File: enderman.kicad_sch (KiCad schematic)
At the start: 22 parts, among them U1 4030, U2 LM556

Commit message: v2.0 RTM
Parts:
- removed R2: 4k7, Resistor_SMD:R_0603_1608Metric, symbol Device:R
- removed R3: 5k1, Resistor_SMD:R_0603_1608Metric, symbol Device:R
- added LS1: Speaker_Crystal, Library:Piezo PKMCS0909E4000-R1, symbol Device:Speaker_Crystal
- added R2, R3: R_Photo, Library:SMD2.4x3.6, symbol Device:R_Photo
- BT1, BT2, BT3: footprint Library:BatteryHolder_Keystone_3030 -> Library:BatteryHolder_Keystone_2996; Digikey 36-3034-ND -> 36-2996-ND
- C2, C5: value 1u -> 47n; LCSC C15849 -> C1622
- D1, D2: LCSC (none) -> C7371915
- U1: LCSC (none) -> C458786
- U2: LCSC (none) -> C18164404
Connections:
- net +6V: now also U1.13, U1.9, R2.1, R3.1; no longer U1.6
- net GND: now also U1.1, U1.2, LS1.2; no longer U1.12, U1.13, U1.8, U1.9
- net at U1.4: now also D1.1 (K), U1.12, U1.8; no longer D2.1 (K)
- net at R1.1, U2.13 (DIS): now also R2.2
- net at U2.9 (Q): now also U1.6; no longer U1.1
- net at R4.1, U2.1 (DIS): now also R3.2
- net at U2.5 (Q): now also U1.5; no longer U1.2
- net at U1.10: now also D2.1 (K)
- net at U1.11: now also LS1.1
- now unconnected: U1.3
- no-connect marks 4 -> 3
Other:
- moved on the sheet: C7, D1, R5, U1A, U1B, U1C, U1D

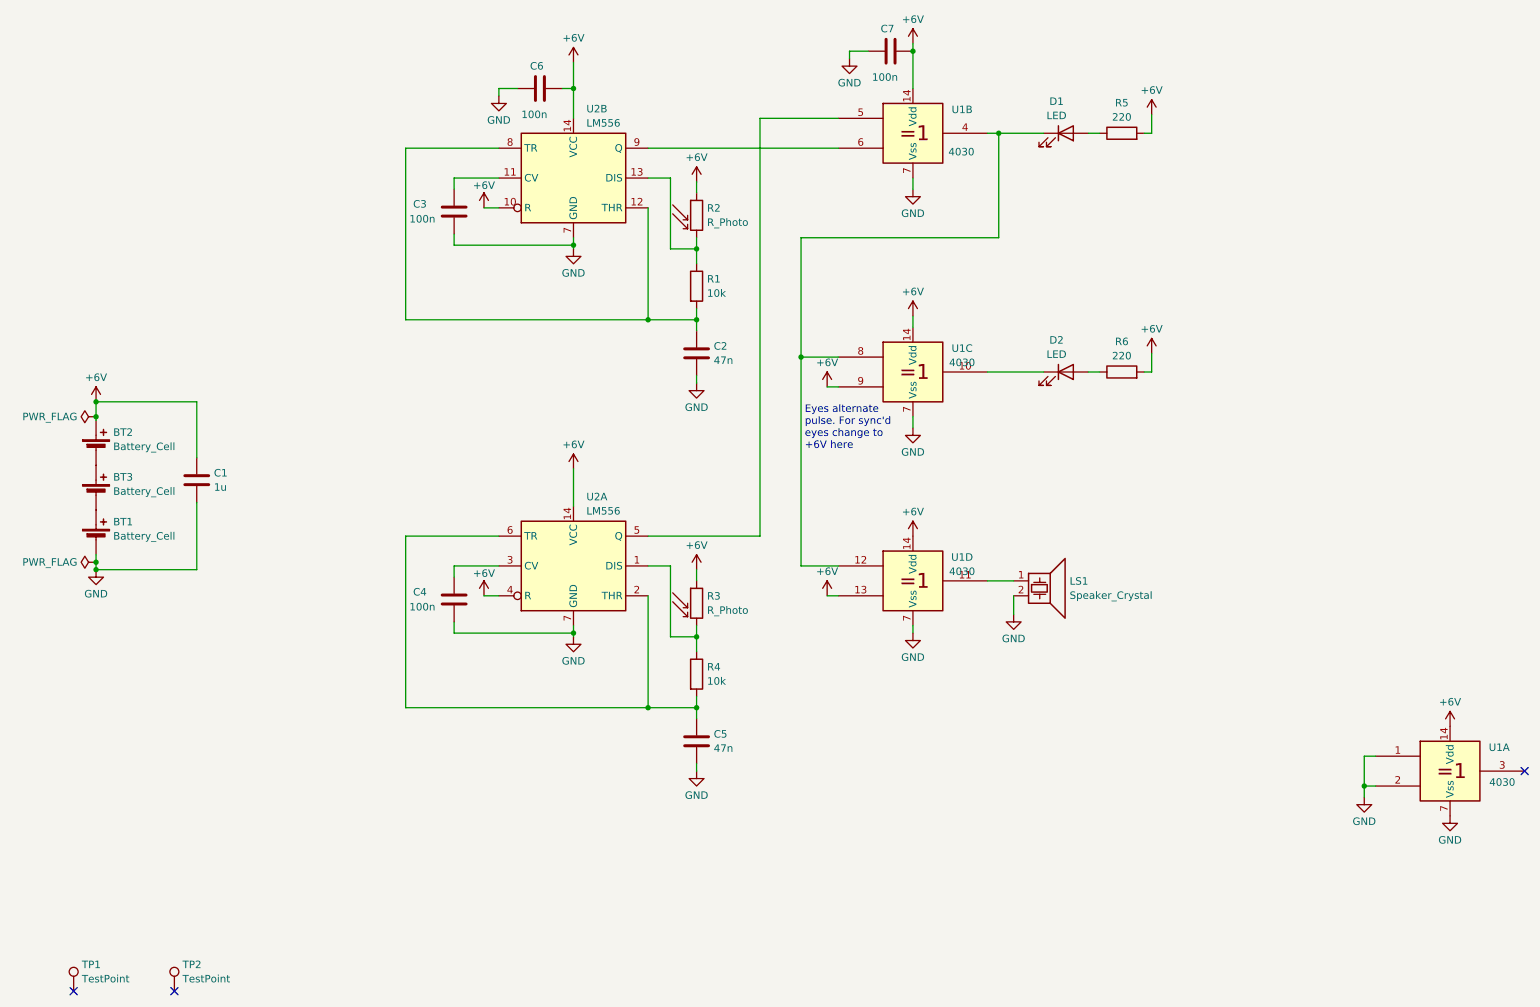
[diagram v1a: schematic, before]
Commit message: routed atari punk console version
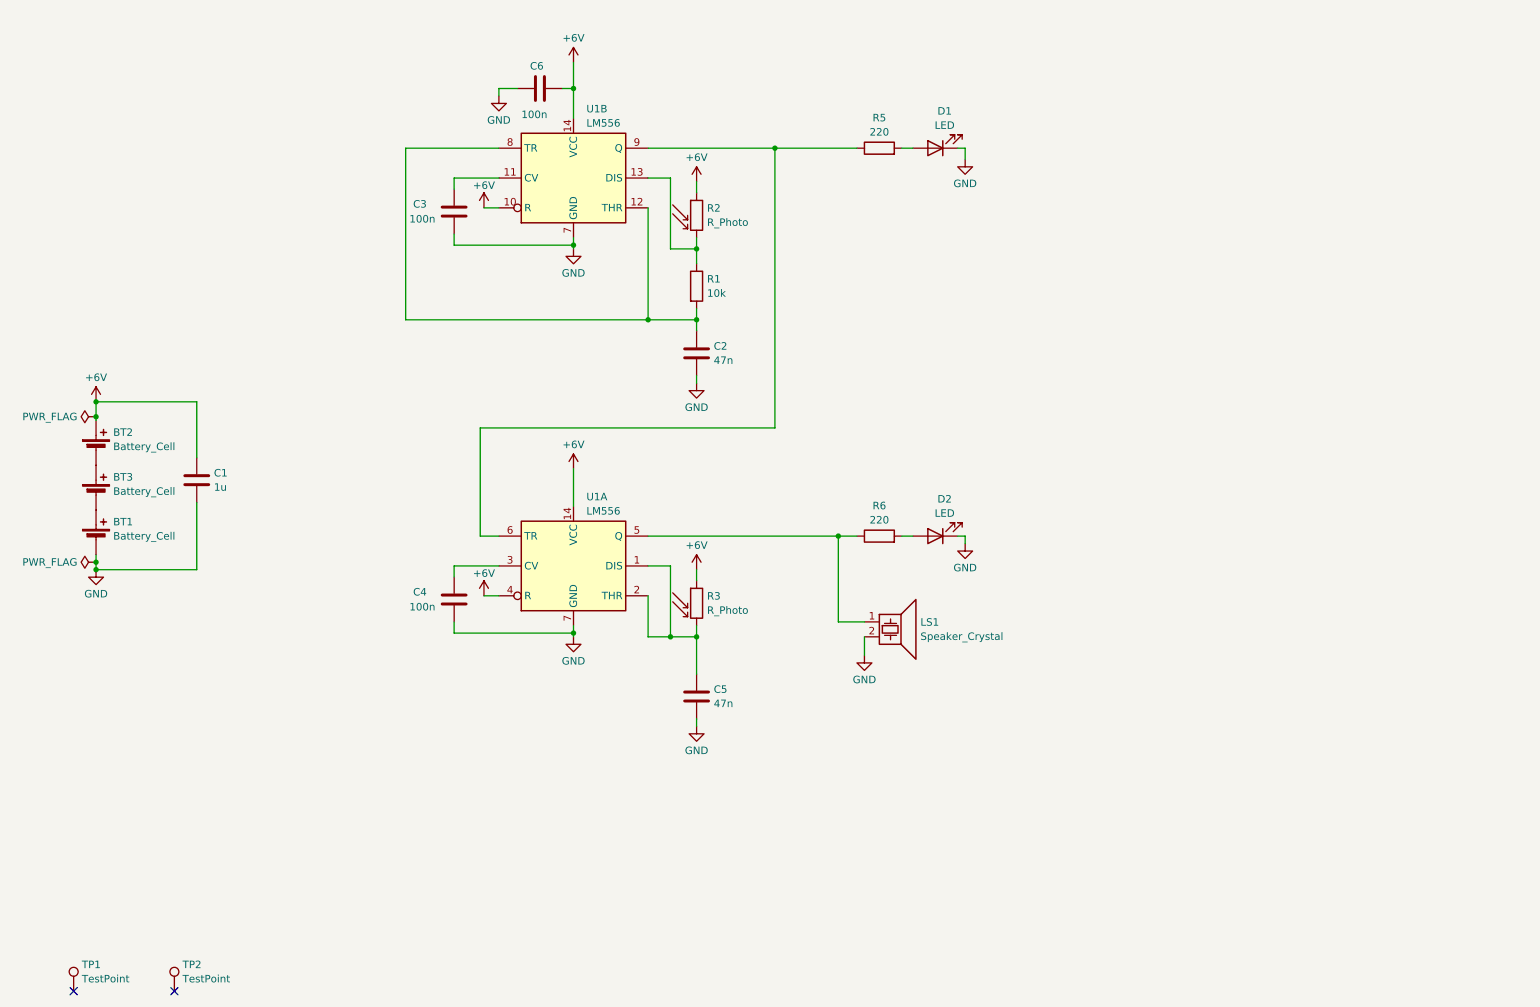
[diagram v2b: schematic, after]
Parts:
- removed C7: 100n, Capacitor_SMD:C_0603_1608Metric, symbol Device:C
- removed R4: 10k, Resistor_SMD:R_0603_1608Metric, symbol Device:R
- removed U1: 4030, Package_SO:SOIC-14_3.9x8.7mm_P1.27mm, symbol 4xxx_IEEE:4030
- renumbered U2 to U1
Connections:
- net +6V: no longer R5.2, R6.2
- net GND: now also D1.1 (K), D2.1 (K)
- net at D1.2 (A): now also R5.2; no longer R5.1
- net at D2.2 (A): now also R6.2; no longer R6.1
- net at U1.9 (Q): now also R5.1, U1.6 (TR)
- net at R3.2, U1.1 (DIS): now also C5.1, U1.2 (THR)
- net at U1.5 (Q): now also LS1.1, R6.1
- no-connect marks 3 -> 2
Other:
- note removed: "Eyes alternate pulse. For sync'd eyes change to +6V here"
- moved on the sheet: C5, D1, D2, LS1, R5, R6

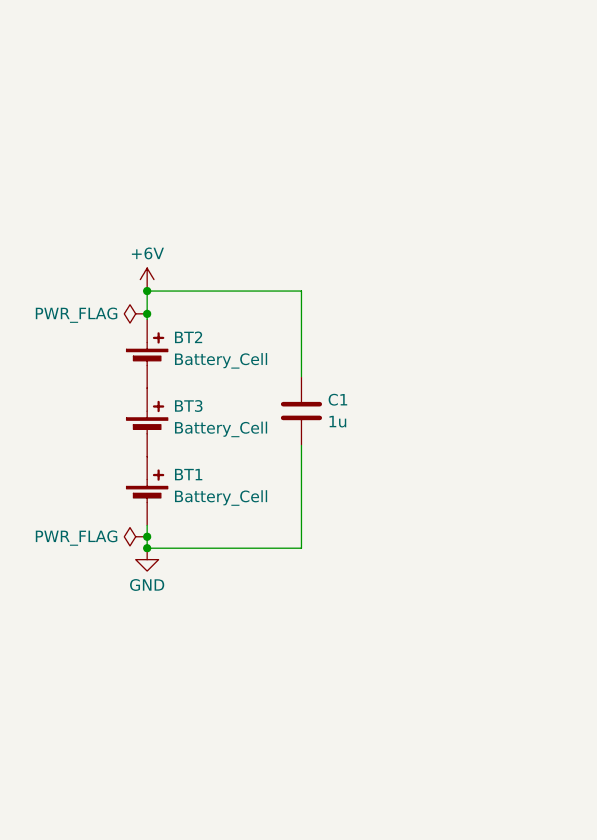
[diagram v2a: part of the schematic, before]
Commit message: updated piezo footprint.  Better routing.  Added on/off switch.  Hid some vias under chip.
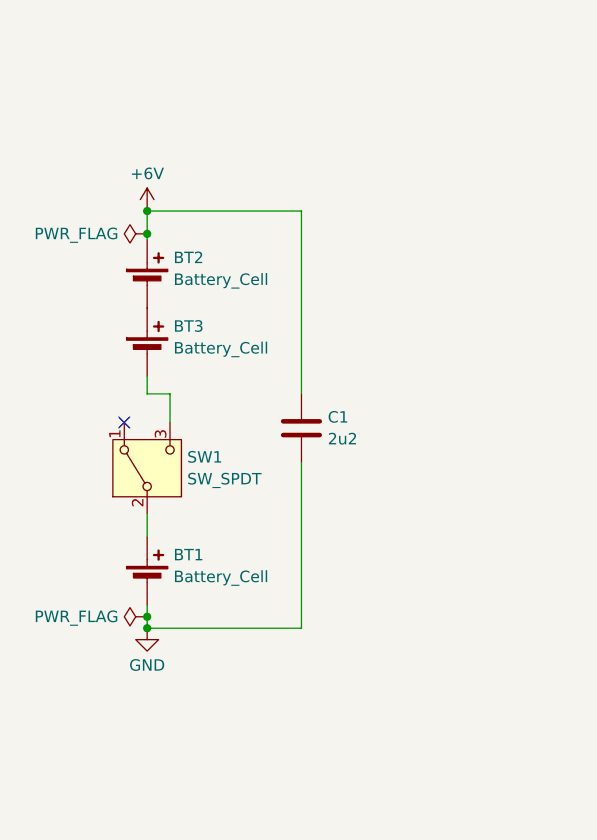
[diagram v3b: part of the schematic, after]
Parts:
- added SW1: SW_SPDT, Button_Switch_SMD:SW_SPDT_PCM12, symbol Switch:SW_SPDT
- C1: value 1u -> 2u2; LCSC C15849 -> (none)
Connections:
- net at BT1.1 (+): now also SW1.2 (B); no longer BT3.2 (-)
- new net: BT3.2 (-), SW1.3 (C)
- no-connect marks 2 -> 3
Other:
- company: (none) -> Reywas Engineering
- title: (none) -> Enderman / Atari Punk Console / Theremin
- moved on the sheet: BT1, BT2, BT3, C1

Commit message: atari punk version
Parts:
- C1: LCSC (none) -> C23630
- R2, R3: LCSC C2904881 -> C2904880
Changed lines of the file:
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@@
       (effects (font (size 1.27 1.27)) hide)
     )
-    (property "LCSC" "C2904881" (at 132.715 51.435 0)
+    (property "LCSC" "C2904880" (at 132.715 51.435 0)
       (effects (font (size 1.27 1.27)) hide)
     )
@@
       (effects (font (size 1.27 1.27)) hide)
     )
-    (property "LCSC" "C2904881" (at 132.715 117.475 0)
+    (property "LCSC" "C2904880" (at 132.715 117.475 0)
       (effects (font (size 1.27 1.27)) hide)
     )
@@
       (effects (font (size 1.27 1.27)) hide)
     )
-    (property "LCSC" "" (at 47.625 98.425 0)
-      (effects (font (size 1.27 1.27)) hide)
-    )
+    (property "LCSC" "C23630" (at 47.625 98.425 0)
+      (effects (font (size 1.27 1.27)) hide)
+    )
